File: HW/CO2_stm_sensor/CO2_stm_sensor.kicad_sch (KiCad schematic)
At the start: 47 parts, among them IC1 SCD41-D-R2, IC2 TPS22917DBVR, IC3 TPS22917DBVR, J1 DM3D-SF(41), J2 SWD, J3 LP_UART, J4 DBG_UART, J5 BATTERY, J6 10118193-0001LF, U1 STM32L021K4T6, U2 TPS7A0228PDBVR

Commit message: gen folder changes
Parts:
- removed C7, C8: 100n, symbol Device:C
- removed R1, R2, R3: 47k, symbol Device:R
- removed UserWakeUp: SW_Push, symbol Switch:SW_Push

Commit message: shchematic v0.0 done
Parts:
- removed C11, C2: 100n, symbol Device:C
- removed C12: 1uF, symbol Device:C
- removed C13: 1nF, symbol Device:C
- removed D2: LED, symbol Device:LED
- removed IC2, IC3: TPS22917DBVR, SOT95P280X145-6N, symbol TPS22917DBVR:TPS22917DBVR
- removed J1: DM3D-SF(41), CONN8_DM3D-SF_HIR, symbol sd_card:DM3D-SF
- removed J5: BATTERY, symbol Connector:Conn_01x02_Socket
- removed J6: 10118193-0001LF, 101181920002LF, symbol 10118192-0002LF:10118192-0002LF
- removed JP2: Jumper, symbol Jumper:Jumper_3_Open
- removed R10: 47k, symbol Device:R
- removed U1: STM32L021K4T6, Package_QFP:LQFP-32_7x7mm_P0.8mm, symbol MCU_ST_STM32L0:STM32L021K4Tx
- removed U3: ~, Package_SON:MicroCrystal_C7_SON-8_1.5x3.2mm_P0.9mm, symbol Timer_RTC:RV-3028-C7
- removed UserWakeUp1: SW_Push, symbol Switch:SW_Push
- added BT1: Battery_Cell, symbol Device:Battery_Cell
- added C11: 100n F, Capacitor_SMD:C_0805_2012Metric_Pad1.18x1.45mm_HandSolder, symbol Device:C_Small
- added C12: 6.8p F, Capacitor_SMD:C_0805_2012Metric_Pad1.18x1.45mm_HandSolder, symbol Device:C_Small
- added C13: 6.8pF, Capacitor_SMD:C_0805_2012Metric_Pad1.18x1.45mm_HandSolder, symbol Device:C_Small
- added C7, C8: 100n F, symbol Device:C
- added C9: 22u F, symbol Device:C
- added J3: SPI, symbol Connector_Generic:Conn_01x06
- added R2: 20K R, symbol Device:R
- added R3: 30k R, symbol Device:R
- added R6: 47k R, symbol Device:R
- added REF1: LDO-AMS1117-3.3, JLC:SOT-223-4_L6.5-W3.5-P2.30-LS7.0-BR, symbol JLC:LDO-AMS1117-3.3
- added SW1: PTS810, Button_Switch_SMD:SW_SPST_PTS810, symbol teser_lib:button
- added U2: P_MOSFET_AO3407A, JLC:SOT-23-3_L2.9-W1.6-P1.90-LS2.8-BR, symbol JLC:P_MOSFET_AO3407A
- added U3: USBC_16PIN, JLC:USB-C-SMD_TYPE-C-6PIN-2MD-073, symbol JLC:USBC_16PIN
- added U4: ESC_Protection_USBLC6-2SC6, JLC:SOT-23-6_L2.9-W1.6-P0.95-LS2.8-BL, symbol JLC:ESC_Protection_USBLC6-2SC6
- added U5: STM32G474RETx, Package_QFP:LQFP-64_10x10mm_P0.5mm, symbol MCU_ST_STM32G4:STM32G474RETx
- added U6: sd_card_slot, JLC:TF-SMD_TF-CARD-H1.8, symbol JLC:sd_card_slot
- added Y1: 24MHz, teser_lib:crystal-24MHz, symbol Device:Crystal_GND24_Small
- C1: value 100n -> 1u F
- C10: value 1uF -> 10u F
- C14: value 1nF -> 100n F
- C15: value 1uF -> 100n F
- C2: renamed from C9; value 1uF -> 2.2u F
- C3: value 100n -> 2.2u F
- C4, C5, C6: value 100n -> 100n F
- J1: renamed from J3; value LP_UART -> UART
- J2: renamed from J4; value DBG_UART -> I2C
- R1: renamed from R6; value 1k -> 2k R
- R4, R5: value 10 -> 10k R
- R7: value 10k -> 47k R
- R8: value 5k -> 47k R
- R9: value 47k -> 47k R
- renumbered H3 to H1, H1 to H2, H4 to H3, H2 to H4, J2 to J4, U2 to U1
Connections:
- net +3.3V is gone; now on net +3V_MCU: J4.1 (Pin_1)
- net 3.1V is gone; now on net +3V_MCU: C5.1, IC1.19 (VDDH)
- net DBG_UART_TX is gone; now on net GND: J2.4 (Pin_4)
- net LP_UART_TX is gone; now on net GND: J1.4 (Pin_4)
- net LP_UART_VDD is gone; now on net +3V_MCU: J1.1 (Pin_1)
- net +3V_MCU: now reaches R7.1
- net +3V_MCU: now also C14.1, C15.1, C3.1, C4.1, C6.1, IC1.7 (VDD), J2.1 (Pin_1), R4.1, R5.1, R8.1, R9.1, C7.1, C8.1, J3.1 (Pin_1), R6.1, U5.1 (VBAT), U5.16 (VDD), U5.28 (VREF+), U5.29 (VDDA), U5.32 (VDD), U5.48 (VDD), U5.64 (VDD), U6.4 (VDD)
- net SD_SPI1_MOSI: now reaches R7.2
- net SD_SPI1_MOSI: now also U5.21 (PA7), U6.3 (CMD)
- net GND: now reaches C4.2
- net GND: now also C1.1, C1.2, C10.2, C14.2, C15.2, C2.2, C3.2, C5.2, C6.2, D1.1 (K), IC1.20 (GND_2), IC1.21 (GND_3), IC1.6 (GND_1), J4.3 (Pin_3), U1.1 (IN), U1.2 (GND), U1.3 (EN), BT1.2 (-), C11.1, C12.2, C13.2, C7.2, C8.2, C9.2, J3.6 (Pin_6), R3.2, SW1.2, U2.1 (G), U2.2 (S), U3.1 (GND), U3.12 (GND), U4.2, U5.15 (VSS), U5.27 (VSSA), U5.31 (VSS), U5.47 (VSS), U5.63 (VSS), U6.10 (GND), U6.11 (GND), U6.12 (GND), U6.13 (GND), U6.6 (VSS), Y1.2, Y1.4
- net at R1.1: now also C10.1, R2.1, REF1.3 (VIN), U3.11 (VBUS), U3.2 (VBUS), U4.5; no longer JP1.1 (A)
- net SD_SPI1_SCK: now reaches R8.2
- net SD_SPI1_SCK: now also U5.19 (PA5), U6.5 (CLK)
- net I2C3_SDA: now reaches J2.3 (Pin_3)
- net I2C3_SDA: now also U5.58 (PB5)
- net USART2_RX: now reaches J1.3 (Pin_3)
- net USART2_RX: now also U5.17 (PA3)
- net at JP1.3 (B): now also C2.1, U1.5 (OUT )
- removed net +3.1V: C14.1, C15.1, C2.1, U1.5 (OUT )
- net DBG_UART_RX renamed I2C3_SCL
- net I2C3_SCL: now also U5.40 (PC8)
- net I2C_SCL renamed CO2_I2C1_SCL
- net CO2_I2C1_SCL: now also R5.2, U5.51 (PA15); no longer R4.1
- net I2C_SDA renamed CO2_I2C1_SDA
- net CO2_I2C1_SDA: now also R4.2, U5.60 (PB7); no longer R5.1
- net LP_UART_RX renamed USART2_TX
- net USART2_TX: now also U5.14 (PA2)
- removed net MCU_POWER: C6.1, IC1.7 (VDD), R4.2, R5.2, R9.2
- net NRST renamed SWD_RST
- net SWD_RST: now also C11.2, SW1.1, U5.7 (PG10); no longer C4.1
- net SWCLK renamed SWD_DIO
- net SWD_DIO: now also U5.49 (PA13)
- net SWDIO renamed SWD_CLK
- net SWD_CLK: now also U5.50 (PA14)
- new net: C13.1, U5.6 (PF1), Y1.1
- new net: C9.1, JP1.1 (A), REF1.2 (VOUT(TAB))
- new net: BT1.1 (+), U2.3 (D)
- new net: C12.1, U5.5 (PF0), Y1.3
- new net: U3.5 (DN2), U3.7 (DN1), U4.1
- new net: U3.6 (DP1), U3.8 (DP2), U4.3
- new net MCU_PWR_ON: U5.12 (PA0)
- new net RTC_I2C2_SCL: U5.43 (PA9)
- new net RTC_I2C2_SDA: U5.42 (PA8)
- new net RTC_INT: U5.13 (PA1)
- new net SD_SPI1_CS: R6.2, U5.18 (PA4), U6.2 (CD/DAT3)
- new net SD_SPI1_MISO: R9.2, U5.20 (PA6), U6.7 (DAT0)
- new net SPI2_CS: J3.2 (Pin_2), U5.34 (PB12)
- new net SPI2_MISO: J3.4 (Pin_4), U5.36 (PB14)
- new net SPI2_MOSI: J3.5 (Pin_5), U5.37 (PB15)
- new net SPI2_SCK: J3.3 (Pin_3), U5.35 (PB13)
- new net USB_DN: U4.6, U5.45 (PA11)
- new net USB_DP: U4.4, U5.46 (PA12)
- new net USB_PWR_SENCE: R2.2, R3.1, U5.44 (PA10)
- new net WakeUp_Circuit/BATTERY_PWR: JP1.2 (C)
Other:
- added sheet WakeUp_Circuit (wakeup_circuit.kicad_sch)
- note added: "CO2_SENSOR"
- note added: "MICRO_SC_CARD_SLOT"
- note added: "SPARE_CONNECTORS"
- note added: "SWD"
- title: (none) -> CO2_stm32_sensor
- moved on the sheet: C2, D1, H1, H2, H3, H4, IC1, J1, J2, J4, JP1, R1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

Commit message: hw v1.0
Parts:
- removed IC1: SCD41-D-R2, SCD41DR2, symbol SCD41-D-R2:SCD41-D-R2
- removed J4: SWD, symbol Connector_Generic:Conn_01x05
- removed SW1: PTS810, Button_Switch_SMD:SW_SPST_PTS810, symbol teser_lib:button
- removed U1: TPS7A0228PDBVR, symbol New_Library_0:LDO_TPS7A02
- added D2, D3: LED, LED_SMD:LED_0805_2012Metric_Pad1.15x1.40mm_HandSolder, symbol Device:LED
- added IC1: SCD41-D-R2, JLC:SCD41DR2, symbol STM32_CO2:SCD41-D-R2
- added J4: Conn_1x6, JLC:CONN-TH_6P-P2.00_S6B-PH-K-S-LF-SN, symbol Connector_Generic:Conn_01x06
- added R15, R16: 5k R, Resistor_SMD:R_0805_2012Metric, symbol Device:R
- added S2: USR_BTN, JLC:pushbutton_EVQPUC02K, symbol CustomSymbols:pushbutton
- added TP2, TP5, TP6, TP7, TP8: TestPoint, Connector_PinHeader_2.54mm:PinHeader_1x01_P2.54mm_Vertical, symbol Connector:TestPoint
- added U8: LDO_TPS7A0228PDBVR, JLC:SOT-23-5_L2.9-W1.6-P0.95-LS2.8-BR, symbol JLC:LDO_TPS7A0228PDBVR
- BT1: footprint (none) -> JLC:BATTERY-SMD_18650-1S-L77.1-W20.7-1; LCSC Part # (none) -> C7525438
- C1, C10, C14, C15, C2, C3, C4, C5, C6, C7, C8, C9: footprint (none) -> Capacitor_SMD:C_0805_2012Metric_Pad1.18x1.45mm_HandSolder
- C12, C13: footprint Capacitor_SMD:C_0805_2012Metric_Pad1.18x1.45mm_HandSolder -> Capacitor_SMD:C_0603_1608Metric_Pad1.08x0.95mm_HandSolder
- D1: footprint (none) -> LED_SMD:LED_0805_2012Metric_Pad1.15x1.40mm_HandSolder
- H1, H2, H3, H4: footprint (none) -> MountingHole:MountingHole_4mm
- J1: value UART -> Conn_1x4; footprint (none) -> JLC:CONN-TH_4P-P2.00_S4B-PH-K-S-LF-SN; LCSC Part # (none) -> C157926
- J2: value I2C -> Conn_1x4; footprint (none) -> JLC:CONN-TH_4P-P2.00_S4B-PH-K-S-LF-SN; LCSC Part # (none) -> C157926
- J3: value SPI -> Conn_1x6; footprint (none) -> JLC:CONN-TH_6P-P2.00_S6B-PH-K-S-LF-SN; LCSC Part # (none) -> C157920
- JP1: footprint (none) -> Connector_PinHeader_2.54mm:PinHeader_1x03_P2.54mm_Vertical; now in the parts list
- R1, R2, R3, R4, R5, R6, R7, R8, R9: footprint (none) -> Resistor_SMD:R_0805_2012Metric
- Y1: footprint teser_lib:crystal-24MHz -> JLC:CRYSTAL-SMD_4P-L2.0-W1.6-BL
- renumbered REF1 to LDO1
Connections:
- net +3V_MCU: now also IC1.19 (VDDH), IC1.7 (VDD), J4.1 (Pin_1)
- net CO2_I2C1_SCL: now also IC1.9 (SCL), TP2.1
- net CO2_I2C1_SDA: now also IC1.10 (SDA), TP5.1
- net GND: now also D2.1 (K), D3.1 (K), IC1.20 (GND_2), IC1.21 (GND_3), IC1.6 (GND_1), J4.3 (Pin_3), S2.4, U8.2 (GND); no longer C1.1, U2.2 (S)
- net I2C3_SCL: now also J2.3 (Pin_3); no longer J2.2 (Pin_2)
- net I2C3_SDA: now also J2.2 (Pin_2); no longer J2.3 (Pin_3)
- net RTC_I2C2_SCL: now also TP6.1
- net RTC_I2C2_SDA: now also TP7.1
- net SWD_CLK: now also J4.4 (Pin_4)
- net SWD_DIO: now also J4.2 (Pin_2)
- net SWD_RST: now also J4.5 (Pin_5), S2.2
- net USART2_RX: now also U5.57 (PB4); no longer U5.17 (PA3)
- net USART2_TX: now also U5.56 (PB3); no longer U5.14 (PA2)
- net at C2.1, JP1.3 (B): now also U8.5 (OUT)
- net at U5.24 (PB0): now also R15.1
- new net: C1.1, TP8.1, U2.2 (S), U8.1 (IN), U8.3 (EN)
- new net: R16.1, U5.17 (PA3)
- new net: D3.2 (A), R16.2
- new net: D2.2 (A), R15.2
- no-connect marks 26 -> 53

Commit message: FIRST ORDER git statusgit status
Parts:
- R1: value 2k R -> 5k R
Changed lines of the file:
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@@
 			)
 		)
-		(property "Value" "2k R"
+		(property "Value" "5k R"
 			(at 46.99 100.33 0)
 			(effects

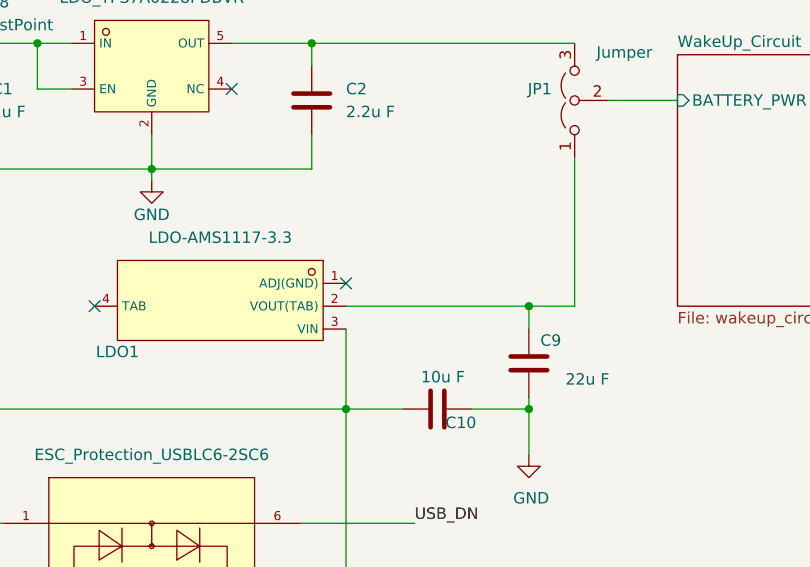
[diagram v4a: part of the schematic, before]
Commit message: LDO GND connected and pwr led rotated in the pcb design
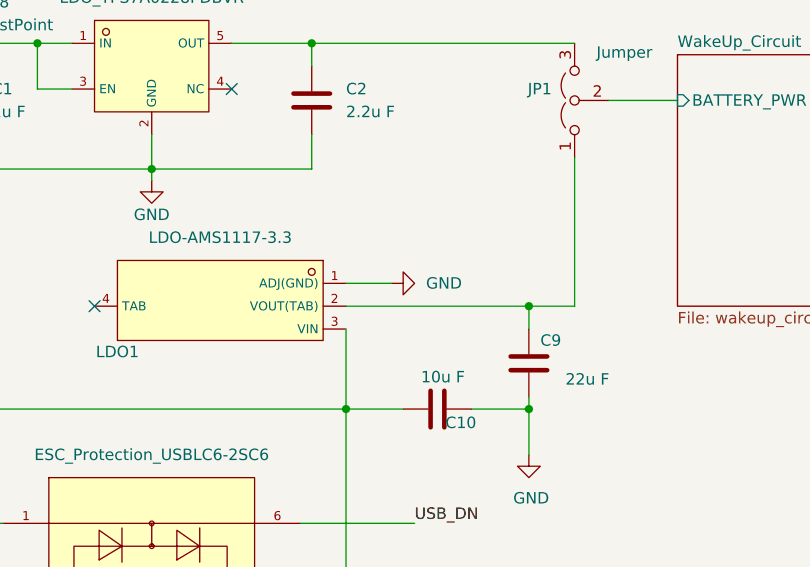
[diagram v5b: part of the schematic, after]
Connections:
- net GND: now also LDO1.1 (ADJ(GND))
- no-connect marks 53 -> 52
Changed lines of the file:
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@@
 	)
 	(no_connect
-		(at 90.17 45.72)
-	)
-	(no_connect
 		(at 224.79 111.76)
 	)
@@
 	(wire
 		(pts
+			(xy 90.17 45.72) (xy 95.25 45.72)
+		)
+		(stroke
+			(width 0)
+			(type default)
+		)
+	)
+	(wire
+		(pts
 			(xy 214.63 71.12) (xy 214.63 83.82)
 		)
@@
 					(unit 1)
 				)
+			)
+		)
+	)
+	(symbol
+		(lib_id "power:GND")
+		(at 95.25 45.72 90)
+		(unit 1)
+		(exclude_from_sim no)
+		(in_bom yes)
+		(on_board yes)
+		(dnp no)
+		(fields_autoplaced yes)
+		(property "Reference" "#PWR043"
+			(at 101.6 45.72 0)
+			(effects
+				(font
+					(size 1.27 1.27)
+				)
+				(hide yes)
+			)
+		)
+		(property "Value" "GND"
+			(at 99.06 45.7199 90)
+			(effects
+				(font
+					(size 1.27 1.27)
+				)
+				(justify right)
+			)
+		)
+		(property "Footprint" ""
+			(at 95.25 45.72 0)
+			(effects
+				(font
+					(size 1.27 1.27)
+				)
+				(hide yes)
+			)
+		)
+		(property "Datasheet" ""
+			(at 95.25 45.72 0)
+			(effects
+				(font
+					(size 1.27 1.27)
+				)
+				(hide yes)
+			)
+		)
+		(property "Description" "Power symbol creates a global label with name \"GND\" , ground"
+			(at 95.25 45.72 0)
+			(effects
+				(font
+					(size 1.27 1.27)
+				)
+				(hide yes)
+			)
+		)
+		(property "LCSC Part #" ""
+			(at 95.25 45.72 0)
+			(effects
+				(font
+					(size 1.27 1.27)
+				)
+				(hide yes)
+			)
+		)
+		(pin "1"
+		)
+		(instances
+			(project "CO2_stm_sensor"
+				(path "/fbf6196a-da46-4b73-a741-a9cbb7111e74"
+					(reference "#PWR043")
+					(unit 1)
+				)

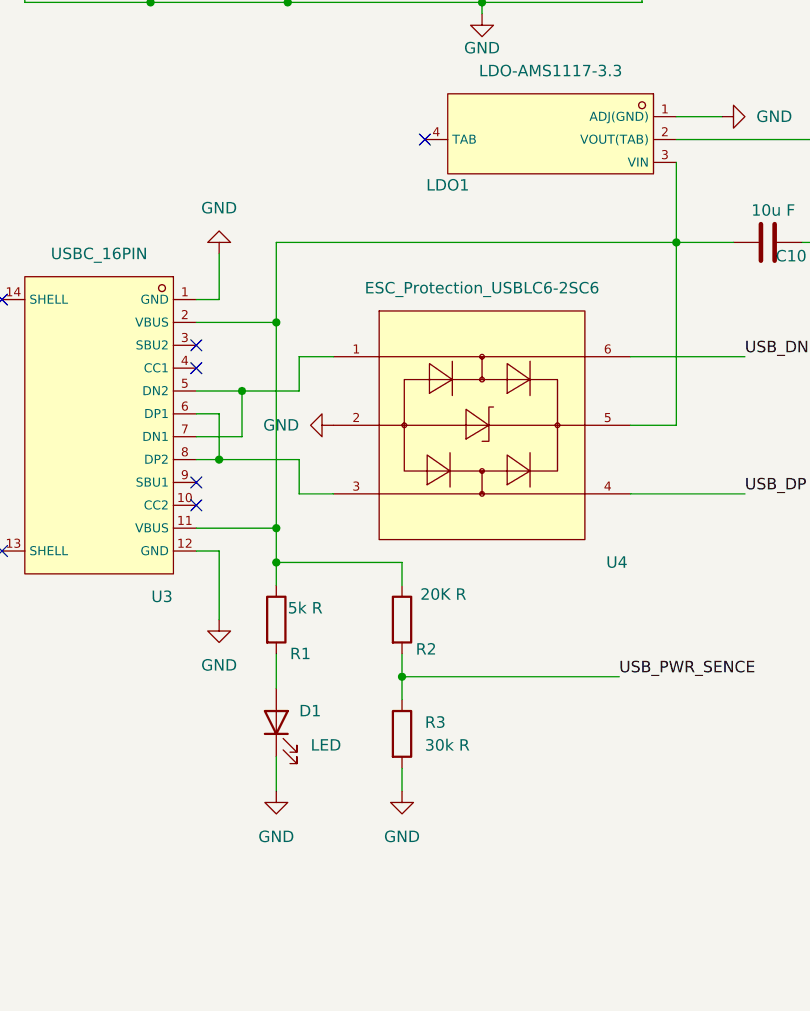
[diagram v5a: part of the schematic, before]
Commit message: add pulldowns to the usb cc1/2 pins
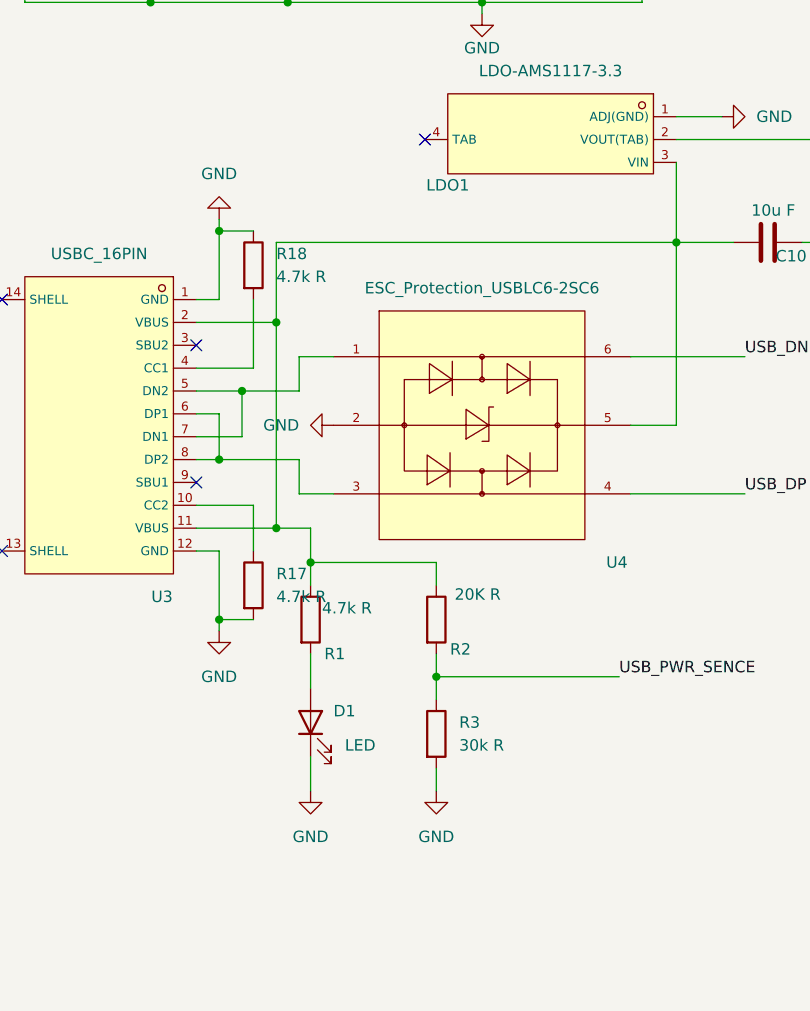
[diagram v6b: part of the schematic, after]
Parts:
- added R17, R18: 4.7k R, symbol Device:R
- R1: value 5k R -> 4.7k R
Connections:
- net GND: now also R17.2, R18.1
- net at U3.10 (CC2): now also R17.1
- net at U3.4 (CC1): now also R18.2
- no-connect marks 52 -> 50
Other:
- moved on the sheet: D1, R1, R2, R3
